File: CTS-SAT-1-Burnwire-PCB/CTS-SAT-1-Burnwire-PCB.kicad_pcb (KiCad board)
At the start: 2 copper layers, 50.8 x 22.9 mm, 28 parts, among them J1 Conn_01x04_MountingPin, J2 Conn_01x06_MountingPin, Q1 AO3400A, Q2 AO3400A

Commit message: Bump version number, add renders, clean up vias through silkscreens
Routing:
- net GND: vias 128 -> 121
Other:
- board text added: "CTS-SAT-1 Boom Burn Wire Rev 2 2025-05-08"
- board text removed: "CTS-SAT-1 Boom Burn Wire Rev 1 2025-03-18"

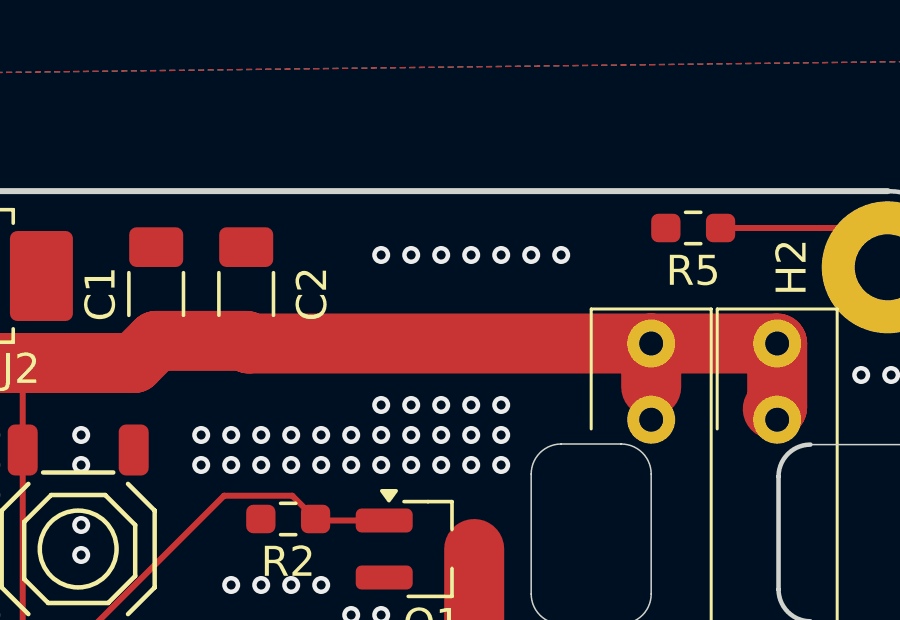
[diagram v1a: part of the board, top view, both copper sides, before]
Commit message: Add power indicator LED
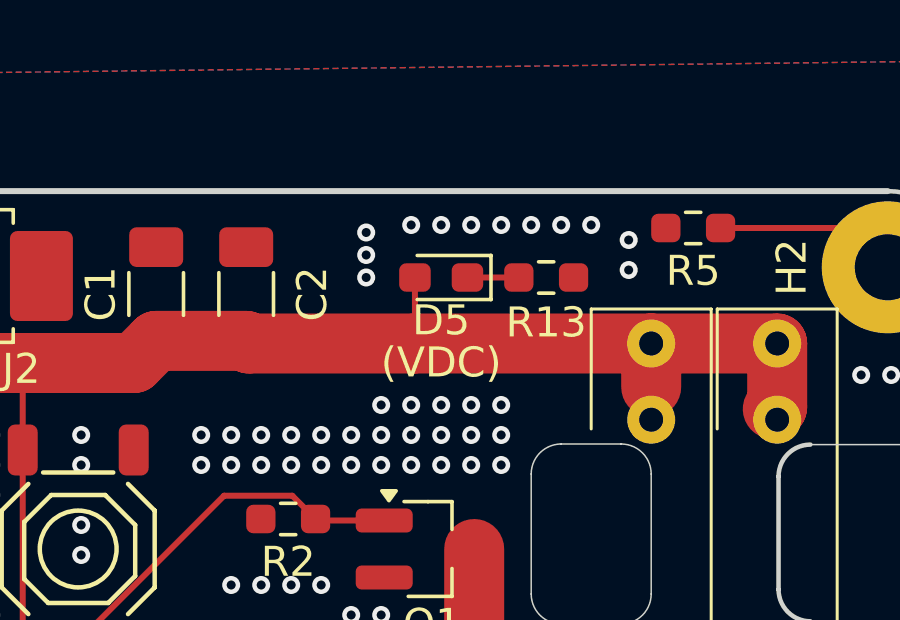
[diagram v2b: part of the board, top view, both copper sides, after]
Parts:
- added D5: LED, LED_SMD:LED_0603_1608Metric_Pad1.05x0.95mm_HandSolder, F.Cu at (109.0, 56.8)
- added R13: 22k, Resistor_SMD:R_0603_1608Metric_Pad0.98x0.95mm_HandSolder, F.Cu at (112.5, 56.8)
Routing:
- net VDC: track 53.8 -> 56.0 mm
- net Net-(D5-K): track 0.00 -> 1.71 mm
- net GND: vias 121 -> 126
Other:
- board text added: "(VDC)"
